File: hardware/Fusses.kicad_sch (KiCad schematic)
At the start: 3 parts

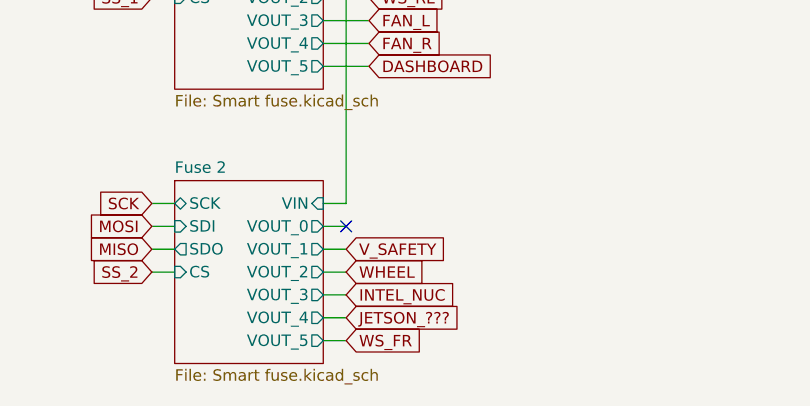
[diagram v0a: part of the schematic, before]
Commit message: changed clock and 5v converter coils, footprints rearrange commponets to fit the need now the board connector is vertical not horizontal relative to the pcb's longest side
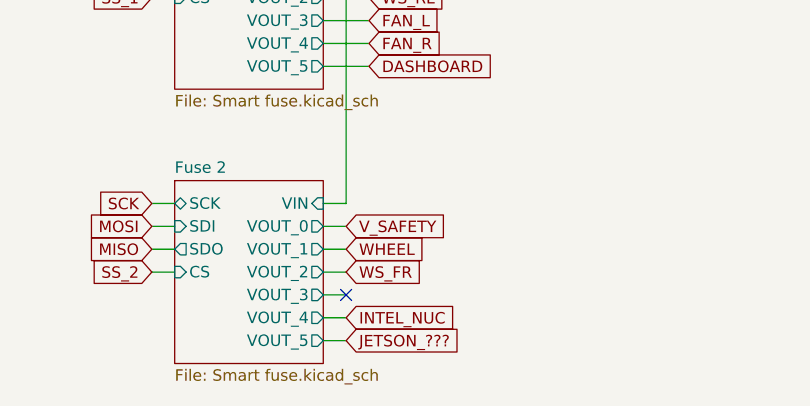
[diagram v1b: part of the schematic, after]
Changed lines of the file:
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@@
   (junction (at 129.54 97.282) (diameter 0) (color 0 0 0 0)
   )
-  (no_connect (at 129.54 130.302))
+  (no_connect (at 129.54 137.922))
   (no_connect (at 77.47 140.462))
   (no_connect (at 77.47 135.382))
@@
     (stroke (width 0) (type default) (color 0 0 0 0))
   )
-  (wire (pts (xy 129.54 130.302) (xy 127 130.302))
+  (wire (pts (xy 129.54 137.922) (xy 127 137.922))
     (stroke (width 0) (type default) (color 0 0 0 0))
   )
@@
     (stroke (width 0) (type default) (color 0 0 0 0))
   )
+  (wire (pts (xy 129.54 132.842) (xy 127 132.842))
+    (stroke (width 0) (type default) (color 0 0 0 0))
+  )
+  (wire (pts (xy 107.95 130.302) (xy 110.49 130.302))
+    (stroke (width 0) (type default) (color 0 0 0 0))
+  )
+  (wire (pts (xy 74.93 127.762) (xy 77.47 127.762))
+    (stroke (width 0) (type default) (color 0 0 0 0))
+  )
+  (wire (pts (xy 132.08 107.442) (xy 127 107.442))
+    (stroke (width 0) (type default) (color 0 0 0 0))
+  )
+  (wire (pts (xy 127 79.502) (xy 132.08 79.502))
+    (stroke (width 0) (type default) (color 0 0 0 0))
+  )
+  (wire (pts (xy 107.95 132.842) (xy 110.49 132.842))
+    (stroke (width 0) (type default) (color 0 0 0 0))
+  )
+  (wire (pts (xy 74.93 143.002) (xy 77.47 143.002))
+    (stroke (width 0) (type default) (color 0 0 0 0))
+  )
+  (wire (pts (xy 129.54 66.802) (xy 129.54 59.182))
+    (stroke (width 0) (type default) (color 0 0 0 0))
+  )
+  (wire (pts (xy 132.08 69.342) (xy 127 69.342))
+    (stroke (width 0) (type default) (color 0 0 0 0))
+  )
+  (wire (pts (xy 129.54 97.282) (xy 129.54 66.802))
+    (stroke (width 0) (type default) (color 0 0 0 0))
+  )
+  (wire (pts (xy 127 140.462) (xy 129.54 140.462))
+    (stroke (width 0) (type default) (color 0 0 0 0))
+  )
+  (wire (pts (xy 107.95 71.882) (xy 110.49 71.882))
+    (stroke (width 0) (type default) (color 0 0 0 0))
+  )
+  (wire (pts (xy 77.47 127.762) (xy 77.47 120.142))
+    (stroke (width 0) (type default) (color 0 0 0 0))
+  )
+  (wire (pts (xy 107.95 69.342) (xy 110.49 69.342))
+    (stroke (width 0) (type default) (color 0 0 0 0))
+  )
+  (wire (pts (xy 55.88 127.762) (xy 58.42 127.762))
+    (stroke (width 0) (type default) (color 0 0 0 0))
+  )
+  (wire (pts (xy 77.47 130.302) (xy 74.93 130.302))
+    (stroke (width 0) (type default) (color 0 0 0 0))
+  )
+  (wire (pts (xy 252.984 114.3) (xy 255.524 114.3))
+    (stroke (width 0) (type default) (color 0 0 0 0))
+  )
+  (wire (pts (xy 107.95 66.802) (xy 110.49 66.802))
+    (stroke (width 0) (type default) (color 0 0 0 0))
+  )
+  (wire (pts (xy 77.47 137.922) (xy 74.93 137.922))
+    (stroke (width 0) (type default) (color 0 0 0 0))
+  )
+  (wire (pts (xy 132.08 104.902) (xy 127 104.902))
+    (stroke (width 0) (type default) (color 0 0 0 0))
+  )
+  (wire (pts (xy 205.994 114.3) (xy 208.534 114.3))
+    (stroke (width 0) (type default) (color 0 0 0 0))
+  )
+  (wire (pts (xy 55.88 135.382) (xy 58.42 135.382))
+    (stroke (width 0) (type default) (color 0 0 0 0))
+  )
+  (wire (pts (xy 127 71.882) (xy 132.08 71.882))
+    (stroke (width 0) (type default) (color 0 0 0 0))
+  )
   (wire (pts (xy 129.54 135.382) (xy 127 135.382))
     (stroke (width 0) (type default) (color 0 0 0 0))
   )
-  (wire (pts (xy 107.95 130.302) (xy 110.49 130.302))
-    (stroke (width 0) (type default) (color 0 0 0 0))
-  )
-  (wire (pts (xy 74.93 127.762) (xy 77.47 127.762))
-    (stroke (width 0) (type default) (color 0 0 0 0))
-  )
-  (wire (pts (xy 132.08 107.442) (xy 127 107.442))
-    (stroke (width 0) (type default) (color 0 0 0 0))
-  )
-  (wire (pts (xy 127 79.502) (xy 132.08 79.502))
-    (stroke (width 0) (type default) (color 0 0 0 0))
-  )
-  (wire (pts (xy 107.95 132.842) (xy 110.49 132.842))
-    (stroke (width 0) (type default) (color 0 0 0 0))
-  )
-  (wire (pts (xy 74.93 143.002) (xy 77.47 143.002))
-    (stroke (width 0) (type default) (color 0 0 0 0))
-  )
-  (wire (pts (xy 129.54 66.802) (xy 129.54 59.182))
-    (stroke (width 0) (type default) (color 0 0 0 0))
-  )
-  (wire (pts (xy 132.08 69.342) (xy 127 69.342))
-    (stroke (width 0) (type default) (color 0 0 0 0))
-  )
-  (wire (pts (xy 129.54 97.282) (xy 129.54 66.802))
-    (stroke (width 0) (type default) (color 0 0 0 0))
-  )
-  (wire (pts (xy 127 137.922) (xy 129.54 137.922))
-    (stroke (width 0) (type default) (color 0 0 0 0))
-  )
-  (wire (pts (xy 107.95 71.882) (xy 110.49 71.882))
-    (stroke (width 0) (type default) (color 0 0 0 0))
-  )
-  (wire (pts (xy 77.47 127.762) (xy 77.47 120.142))
-    (stroke (width 0) (type default) (color 0 0 0 0))
-  )
-  (wire (pts (xy 107.95 69.342) (xy 110.49 69.342))
-    (stroke (width 0) (type default) (color 0 0 0 0))
-  )
-  (wire (pts (xy 55.88 127.762) (xy 58.42 127.762))
-    (stroke (width 0) (type default) (color 0 0 0 0))
-  )
-  (wire (pts (xy 77.47 130.302) (xy 74.93 130.302))
-    (stroke (width 0) (type default) (color 0 0 0 0))
-  )
-  (wire (pts (xy 252.984 114.3) (xy 255.524 114.3))
-    (stroke (width 0) (type default) (color 0 0 0 0))
-  )
-  (wire (pts (xy 107.95 66.802) (xy 110.49 66.802))
-    (stroke (width 0) (type default) (color 0 0 0 0))
-  )
-  (wire (pts (xy 77.47 137.922) (xy 74.93 137.922))
-    (stroke (width 0) (type default) (color 0 0 0 0))
-  )
-  (wire (pts (xy 132.08 104.902) (xy 127 104.902))
-    (stroke (width 0) (type default) (color 0 0 0 0))
-  )
-  (wire (pts (xy 205.994 114.3) (xy 208.534 114.3))
-    (stroke (width 0) (type default) (color 0 0 0 0))
-  )
-  (wire (pts (xy 55.88 135.382) (xy 58.42 135.382))
-    (stroke (width 0) (type default) (color 0 0 0 0))
-  )
-  (wire (pts (xy 127 71.882) (xy 132.08 71.882))
-    (stroke (width 0) (type default) (color 0 0 0 0))
-  )
-  (wire (pts (xy 129.54 143.002) (xy 127 143.002))
-    (stroke (width 0) (type default) (color 0 0 0 0))
-  )
   (wire (pts (xy 195.834 97.028) (xy 198.374 97.028))
     (stroke (width 0) (type default) (color 0 0 0 0))
@@
     (stroke (width 0) (type default) (color 0 0 0 0))
   )
-  (wire (pts (xy 127 140.462) (xy 129.54 140.462))
+  (wire (pts (xy 127 143.002) (xy 129.54 143.002))
     (stroke (width 0) (type default) (color 0 0 0 0))
   )
@@
     (stroke (width 0) (type default) (color 0 0 0 0))
   )
-  (wire (pts (xy 127 132.842) (xy 129.54 132.842))
+  (wire (pts (xy 127 130.302) (xy 129.54 130.302))
     (stroke (width 0) (type default) (color 0 0 0 0))
   )
@@
     )
   )
-  (global_label "WHEEL" (shape input) (at 129.54 135.382 0) (fields_autoplaced)
-    (effects (font (size 1.27 1.27)) (justify left))
-    (property "Intersheet References" "${INTERSHEET_REFS}" (id 0) (at -430.53 31.242 0)
+  (global_label "WHEEL" (shape input) (at 129.54 132.842 0) (fields_autoplaced)
+    (effects (font (size 1.27 1.27)) (justify left))
+    (property "Intersheet References" "${INTERSHEET_REFS}" (id 0) (at -430.53 28.702 0)
       (effects (font (size 1.27 1.27)) hide)
     )
@@
     )
   )
-  (global_label "V_SAFETY" (shape input) (at 129.54 132.842 0) (fields_autoplaced)
-    (effects (font (size 1.27 1.27)) (justify left))
-    (property "Intersheet References" "${INTERSHEET_REFS}" (id 0) (at -430.53 31.242 0)
+  (global_label "V_SAFETY" (shape input) (at 129.54 130.302 0) (fields_autoplaced)
+    (effects (font (size 1.27 1.27)) (justify left))
+    (property "Intersheet References" "${INTERSHEET_REFS}" (id 0) (at -430.53 28.702 0)
       (effects (font (size 1.27 1.27)) hide)
     )
@@
     )
   )
-  (global_label "JETSON_???" (shape input) (at 129.54 140.462 0) (fields_autoplaced)
-    (effects (font (size 1.27 1.27)) (justify left))
-    (property "Intersheet References" "${INTERSHEET_REFS}" (id 0) (at -430.53 31.242 0)
+  (global_label "JETSON_???" (shape input) (at 129.54 143.002 0) (fields_autoplaced)
+    (effects (font (size 1.27 1.27)) (justify left))
+    (property "Intersheet References" "${INTERSHEET_REFS}" (id 0) (at -430.53 33.782 0)
       (effects (font (size 1.27 1.27)) hide)
     )
@@
     )
   )
-  (global_label "WS_FR" (shape input) (at 129.54 143.002 0) (fields_autoplaced)
-    (effects (font (size 1.27 1.27)) (justify left))
-    (property "Intersheet References" "${INTERSHEET_REFS}" (id 0) (at -430.53 31.242 0)
-      (effects (font (size 1.27 1.27)) hide)
-    )
-  )
-  (global_label "INTEL_NUC" (shape input) (at 129.54 137.922 0) (fields_autoplaced)
-    (effects (font (size 1.27 1.27)) (justify left))
-    (property "Intersheet References" "${INTERSHEET_REFS}" (id 0) (at -430.53 31.242 0)
-      (effects (font (size 1.27 1.27)) hide)
-    )
+  (global_label "WS_FR" (shape input) (at 129.54 135.382 0) (fields_autoplaced)
+    (effects (font (size 1.27 1.27)) (justify left))
+    (property "Intersheet References" "${INTERSHEET_REFS}" (id 0) (at -430.53 23.622 0)
+      (effects (font (size 1.27 1.27)) hide)
+    )
+  )
+  (global_label "INTEL_NUC" (shape input) (at 129.54 140.462 0) (fields_autoplaced)
+    (effects (font (size 1.27 1.27)) (justify left))
+    (property "Intersheet References" "${INTERSHEET_REFS}" (id 0) (at -430.53 33.782 0)
+      (effects (font (size 1.27 1.27)) hide)
+    )

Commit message: minor improvements
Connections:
- no-connect marks 6 -> 3
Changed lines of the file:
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@@
   )
   (no_connect (at 129.54 137.922))
-  (no_connect (at 77.47 140.462))
-  (no_connect (at 77.47 135.382))
   (no_connect (at 77.47 132.842))
   (no_connect (at 77.47 130.302))
-  (no_connect (at 77.47 137.922))
   (wire (pts (xy 242.824 114.3) (xy 245.364 114.3))
     (stroke (width 0) (type default) (color 0 0 0 0))
@@
     )
   )
+  (global_label "V_SPARE_3" (shape input) (at 77.47 140.462 0) (fields_autoplaced)
+    (effects (font (size 1.27 1.27)) (justify left))
+    (property "Intersheet References" "${INTERSHEET_REFS}" (id 0) (at 90.0147 140.3826 0)
+      (effects (font (size 1.27 1.27)) (justify left) hide)
+    )
+  )
+  (global_label "V_SPARE_1" (shape input) (at 77.47 135.382 0) (fields_autoplaced)
+    (effects (font (size 1.27 1.27)) (justify left))
+    (property "Intersheet References" "${INTERSHEET_REFS}" (id 0) (at 90.0147 135.3026 0)
+      (effects (font (size 1.27 1.27)) (justify left) hide)
+    )
+  )
   (global_label "FAN_L" (shape input) (at 132.08 107.442 0) (fields_autoplaced)
     (effects (font (size 1.27 1.27)) (justify left))
@@
     )
   )
+  (global_label "V_SPARE_2" (shape input) (at 77.47 137.922 0) (fields_autoplaced)
+    (effects (font (size 1.27 1.27)) (justify left))
+    (property "Intersheet References" "${INTERSHEET_REFS}" (id 0) (at 90.0147 137.8426 0)
+      (effects (font (size 1.27 1.27)) (justify left) hide)
+    )
+  )

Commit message: fuck
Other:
- note added: "odrive zamiast dashboarda 8 9 10 dashboard na spara_2"
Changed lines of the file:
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@@
     (effects (font (size 2.9972 2.9972) (thickness 0.5994) bold) (justify right bottom))
+  )
+  (text "odrive zamiast dashboarda\n8\n9\n10\ndashboard na spara_2"
+    (at 147.32 115.57 0)
+    (effects (font (size 1.27 1.27)) (justify left bottom))
   )
   (global_label "V_BSPD" (shape input) (at 208.534 97.028 0) (fields_autoplaced)

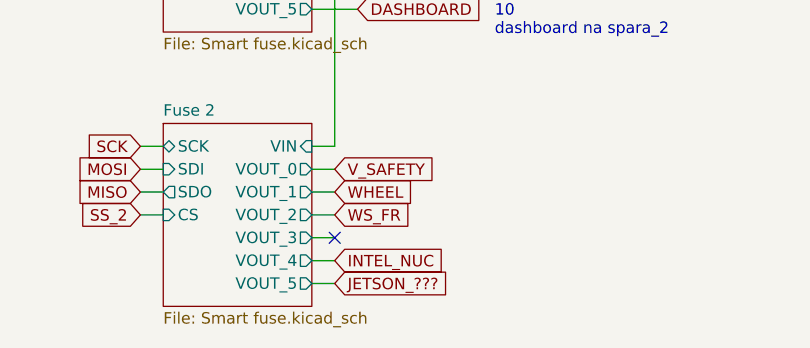
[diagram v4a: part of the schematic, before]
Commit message: currected sf autosport connector, also updated firmware to better handle the showing of board status throught the on board LEDs
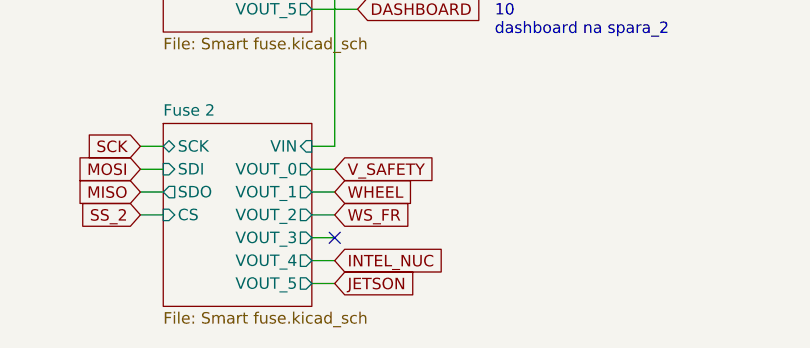
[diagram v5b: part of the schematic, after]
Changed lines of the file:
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@@
     )
   )
-  (global_label "JETSON_???" (shape input) (at 129.54 143.002 0) (fields_autoplaced)
+  (global_label "JETSON" (shape input) (at 129.54 143.002 0) (fields_autoplaced)
     (effects (font (size 1.27 1.27)) (justify left))
-    (property "Intersheet References" "${INTERSHEET_REFS}" (id 0) (at -430.53 33.782 0)
-      (effects (font (size 1.27 1.27)) hide)
+    (property "Intersheet References" "${INTERSHEET_REFS}" (id 0) (at 138.819 142.9226 0)
+      (effects (font (size 1.27 1.27)) (justify left) hide)
     )
   )

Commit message: major schematic update, changed optocouplers for different, added new fuses for 5v supply for water and potentiometers and 24v supply for BSPD/ESB, updated autosport connector, and some other changes
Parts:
- removed F1, F2, F4: Polyfuse, Fuse:Fuse_2010_5025Metric, symbol Device:Polyfuse
- added D10, D9: D_SCH, Diode_SMD:D_0603_1608Metric, symbol Device:D_Schottky_Small
- added R17, R18, R41, R42: R_Small, Resistor_SMD:R_0603_1608Metric, symbol Device:R_Small
- added U16, U17: FOD8802DR2, SOIC127P600X175-8N, symbol FOD8802DR2:FOD8802DR2
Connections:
- new net: D9.1 (K), R17.1, U16.1 (ANODE_1)
- new net: D10.1 (K), R18.1, U16.3 (ANODE_2)
- new net +3V3: U16.8 (COLLECTOR_1)
- new net +5V: U16.6 (COLLECTOR_2)
- new net GND: D10.2 (A), D9.2 (A), R41.1, R42.1, U16.2 (CATHODE_1), U16.4 (CATHODE_2)
- new net WATER/POT_EN: R42.2, U16.5 (EMITTER_2)
- new net WATER/POT_ENABLE: R18.2
- new net WATER/POT_FLAG: R17.2
- new net WATER/POT_STATE: R41.2, U16.7 (EMITTER_1)
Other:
- added sheet BSPD-ESB (eFuse 24V.kicad_sch)
- added sheet WATER-POTENTIOMMETER (eFuse 5V.kicad_sch)
- note removed: "odrive zamiast dashboarda 8 9 10 dashboard na spara_2"

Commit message: changed some footprints for clarity, and made some progress on board
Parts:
- removed D10, D9: D_SCH, Diode_SMD:D_0603_1608Metric, symbol Device:D_Schottky_Small
- removed R17, R18, R41, R42: R_Small, Resistor_SMD:R_0603_1608Metric, symbol Device:R_Small
- removed U16, U17: FOD8802DR2, SOIC127P600X175-8N, symbol FOD8802DR2:FOD8802DR2
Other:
- added sheet Supply (eFuse supply 24V.kicad_sch)
- note added: "Smart Fuses 24V"
- note added: "eFuses 24V"
- note added: "eFuses 5V"
- note removed: "Fuses"

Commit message: finished new wersion of the board
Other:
- added sheet TSAL (eFuse 24V TSAL.kicad_sch)
- sheet BSPD-ESB: file eFuse 24V.kicad_sch -> eFuse 24V BSPD-ESB.kicad_sch
- sheet WATER-POTENTIOMMETER ports: added ~{ENABLE}; removed ~{EN}
